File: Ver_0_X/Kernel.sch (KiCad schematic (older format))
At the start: 14 parts, among them J1 TTL, J2 L, J3 R, J4 TTL, SW1 MODE, SW2 Reset, SW3 RePair, U1 ESP-12S

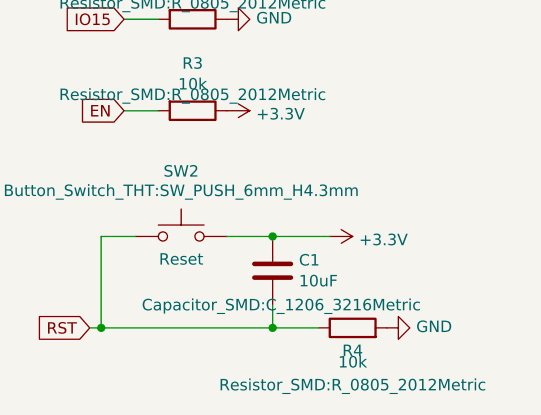
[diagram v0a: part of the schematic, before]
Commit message: fixed reset
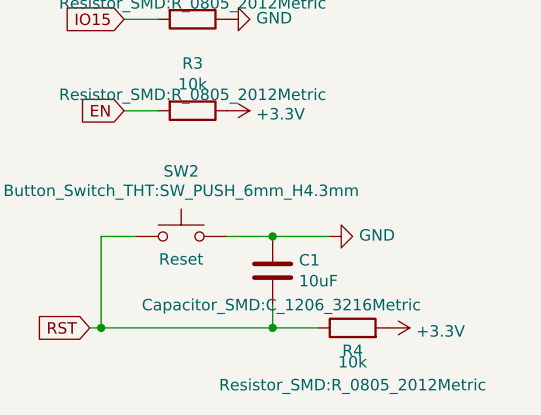
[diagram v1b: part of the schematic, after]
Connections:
- net +3V3: now also R4.2; no longer C1.1, SW2.2
- net GND: now also C1.1, SW2.2; no longer R4.2
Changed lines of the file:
@@
 L power:+3.3V #PWR0107
 U 1 1 60495940
-P 7900 4650
-F 0 "#PWR0107" H 7900 4500 50  0001 C CNN
-F 1 "+3.3V" V 7915 4778 50  0000 L CNN
-F 2 "" H 7900 4650 50  0001 C CNN
-F 3 "" H 7900 4650 50  0001 C CNN
-	1    7900 4650
+P 8150 5050
+F 0 "#PWR0107" H 8150 4900 50  0001 C CNN
+F 1 "+3.3V" V 8165 5178 50  0000 L CNN
+F 2 "" H 8150 5050 50  0001 C CNN
+F 3 "" H 8150 5050 50  0001 C CNN
+	1    8150 5050
 	0    1    1    0
 $EndComp
@@
 L power:GND #PWR0108
 U 1 1 604962A2
-P 8150 5050
-F 0 "#PWR0108" H 8150 4800 50  0001 C CNN
-F 1 "GND" V 8155 4922 50  0000 R CNN
-F 2 "" H 8150 5050 50  0001 C CNN
-F 3 "" H 8150 5050 50  0001 C CNN
-	1    8150 5050
+P 7900 4650
+F 0 "#PWR0108" H 7900 4400 50  0001 C CNN
+F 1 "GND" V 7905 4522 50  0000 R CNN
+F 2 "" H 7900 4650 50  0001 C CNN
+F 3 "" H 7900 4650 50  0001 C CNN
+	1    7900 4650
 	0    -1   -1   0
 $EndComp
